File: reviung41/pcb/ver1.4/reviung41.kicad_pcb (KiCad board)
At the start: 2 copper layers, 253.3 x 107.1 mm, 111 parts, among them SW1 SW_PUSH, SW10 SW_PUSH, SW11 SW_PUSH, SW12 SW_PUSH, SW13 SW_PUSH, SW14 SW_PUSH, SW15 SW_PUSH, SW16 SW_PUSH, SW17 SW_PUSH, SW18 SW_PUSH, SW19 SW_PUSH, SW2 SW_PUSH, SW20 SW_PUSH, SW21 SW_PUSH, SW22 SW_PUSH, SW23 SW_PUSH, SW24 SW_PUSH, SW25 SW_PUSH, SW26 SW_PUSH, SW27 SW_PUSH, SW28 SW_PUSH, SW29 SW_PUSH, SW3 SW_PUSH, SW30 SW_PUSH, SW31 SW_PUSH, SW32 SW_PUSH, SW33 SW_PUSH, SW34 SW_PUSH, SW35 SW_PUSH, SW36 SW_PUSH, SW37 SW_PUSH, SW38 SW_PUSH, SW39 SW_2U_PUSH, SW4 SW_PUSH, SW40 SW_PUSH, SW41 SW_PUSH, SW5 SW_PUSH, SW6 SW_PUSH, SW7 SW_PUSH, SW8 SW_PUSH, SW9 SW_PUSH, U1 ProMicro

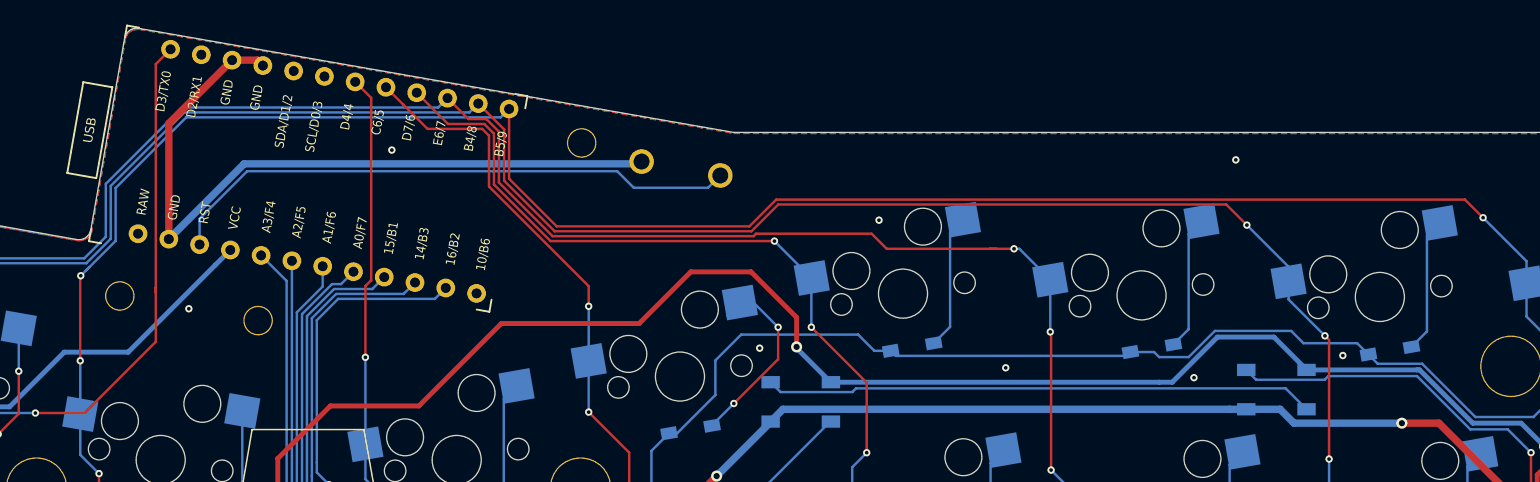
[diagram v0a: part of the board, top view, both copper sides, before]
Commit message: add oled and switch, hole for battery
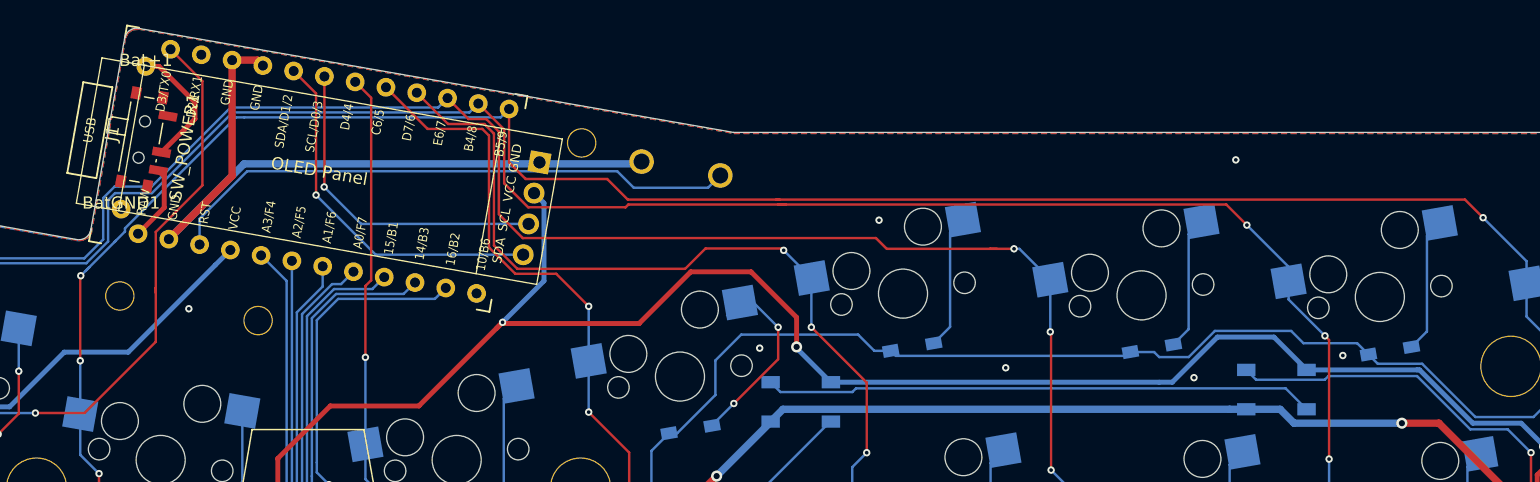
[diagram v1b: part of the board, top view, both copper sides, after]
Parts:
- added Bat+1: MountingHole_Pad, rev:batteryhole, F.Cu at (131.5, 53.2)
- added BatGND1: MountingHole_Pad, rev:batteryhole, F.Cu at (129.5, 64.8)
- added J1: OLED-128x32, rev:SSD1306-0.91-OLED-4pin-128x32, F.Cu at (127.9, 52.5)
- added SW_POWER1: SW_SPDT, Button_Switch_SMD:SW_SPDT_PCM12, F.Cu at (131.5, 59.2)
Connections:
- L11 pad 2: (no net) -> unconnected-(L11-DOUT-Pad2)
- U1 pad 13: (no net) -> unconnected-(U1-B6/10-Pad13)
- U1 pad 2: (no net) -> unconnected-(U1-RX1/D2-Pad2)
- U1 pad 24: (no net) -> raw
- U1 pad 5: (no net) -> SDA
- U1 pad 6: (no net) -> SCL
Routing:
- net SDA: track 0.00 -> 29.7 mm, vias 0 -> 1
- net SCL: track 0.00 -> 26.9 mm, vias 0 -> 1
- net VCC: track 552.4 -> 568.4 mm, vias 11 -> 12
- net BT+: track 0.00 -> 10.4 mm
- net raw: track 0.00 -> 6.22 mm
- net col5: track 231.4 -> 226.8 mm
- net col2: track 312.8 -> 317.1 mm
- net LED: track 58.3 -> 60.4 mm
- net col1: track 289.5 -> 291.5 mm
- net col4: track 269.1 -> 267.7 mm
- net col3: track 278.1 -> 278.9 mm
- net GND: vias 61 -> 60
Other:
- net class Default removed
